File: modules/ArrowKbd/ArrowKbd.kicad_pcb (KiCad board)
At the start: 2 copper layers, 40.6 x 40.6 mm, 42 parts, among them J1 2, J10 11, J11 12, J12 13, J13 A0, J14 A1, J15 A2, J16 A3, J17 A4, J18 A5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

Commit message: ArrowKbd v2. Change pin assigning
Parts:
- moved JP1 20.2 mm to (120.7, 84.8), turned to 270 degrees
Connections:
- JP1 pad 1: Net-(J8-Pad1) -> Net-(J6-Pad1)
- JP1 pad 3: Net-(J7-Pad1) -> Net-(J3-Pad1)
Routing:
- net Net-(J6-Pad1): track 0.00 -> 20.9 mm
- net Net-(J3-Pad1): track 0.00 -> 20.4 mm
- net Net-(JP1-Pad2): track 55.9 -> 41.8 mm
- net Net-(J7-Pad1): track 3.59 -> 0.00 mm
- net Net-(J8-Pad1): track 2.54 -> 0.00 mm
- net Net-(D1-Pad2): track 37.9 -> 37.4 mm
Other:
- board text added: "hash"
- board text added: "v2"

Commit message: ArrowKbd. Add photomask in pdf.
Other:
- board text added: "c62680"
- board text removed: "hash"
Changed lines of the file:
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@@
     )
   )
-  (gr_text hash (at 117.475 89.2175) (layer F.Cu)
-    (effects (font (size 1.5 1.5) (thickness 0.3)))
+  (gr_text c62680 (at 118.11 89.2175) (layer F.Cu)
+    (effects (font (size 1 1) (thickness 0.2)))
   )
   (gr_text v2 (at 98.425 89.2175) (layer F.Cu)

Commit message: ArrowKbd. Update photomask in pdf.
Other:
- board text added: "747176"
- board text removed: "c62680"
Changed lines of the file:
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@@
     (visible_elements 7FFFFFFF)
     (pcbplotparams
-      (layerselection 0x010fc_ffffffff)
+      (layerselection 0x00000_fffffffe)
       (usegerberextensions false)
       (usegerberattributes false)
@@
       (hpglpenspeed 20)
       (hpglpendiameter 15.000000)
-      (psnegative false)
+      (psnegative true)
       (psa4output false)
       (plotreference true)
@@
       (padsonsilk false)
       (subtractmaskfromsilk false)
-      (outputformat 1)
+      (outputformat 4)
       (mirror false)
-      (drillshape 0)
+      (drillshape 1)
       (scaleselection 1)
-      (outputdirectory "arrowkbd/"))
+      (outputdirectory "pdf/"))
   )
   (net 0 "")
@@
     )
   )
-  (gr_text c62680 (at 118.11 89.2175) (layer F.Cu)
+  (gr_text 747176 (at 118.11 89.2175) (layer F.Cu)
     (effects (font (size 1 1) (thickness 0.2)))
   )

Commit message: ArrowKbd polishing
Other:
- board text added: "07.05.2020"
- board text added: "138553"
- board text removed: "04.03.2020"
- board text removed: "747176"
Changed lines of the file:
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@@
   )
   (setup
-    (last_trace_width 0.6)
+    (last_trace_width 0.25)
     (user_trace_width 0.4)
     (user_trace_width 0.5)
@@
     (mod_text_size 1 1)
     (mod_text_width 0.15)
-    (pad_size 1.524 1.524)
-    (pad_drill 0.762)
+    (pad_size 2 2)
+    (pad_drill 1)
     (pad_to_mask_clearance 0.051)
     (solder_mask_min_width 0.25)
@@
       (effects (font (size 1 1) (thickness 0.15)))
     )
-    (pad 1 thru_hole rect (at 0 0 270) (size 1.7 1.7) (drill 1) (layers *.Cu *.Mask)
+    (pad 1 thru_hole rect (at 0 0 270) (size 2 2) (drill 1) (layers *.Cu *.Mask)
       (net 6 "Net-(J6-Pad1)"))
-    (pad 2 thru_hole oval (at 0 2.54 270) (size 1.7 1.7) (drill 1) (layers *.Cu *.Mask)
+    (pad 2 thru_hole oval (at 0 2.54 270) (size 2 2) (drill 1) (layers *.Cu *.Mask)
       (net 29 "Net-(JP1-Pad2)"))
-    (pad 3 thru_hole oval (at 0 5.08 270) (size 1.7 1.7) (drill 1) (layers *.Cu *.Mask)
+    (pad 3 thru_hole oval (at 0 5.08 270) (size 2 2) (drill 1) (layers *.Cu *.Mask)
       (net 3 "Net-(J3-Pad1)"))
     (model ${KISYS3DMOD}/Connector_PinHeader_2.54mm.3dshapes/PinHeader_1x03_P2.54mm_Vertical.wrl
@@
     )
   )
-  (gr_text 747176 (at 118.11 89.2175) (layer F.Cu)
+  (gr_text 138553 (at 118.11 89.2175) (layer F.Cu)
     (effects (font (size 1 1) (thickness 0.2)))
   )
@@
   )
   (gr_poly (pts (xy 114.01 62.12) (xy 114.72 63.14) (xy 114.94 63.46) (xy 115.13 63.64) (xy 115.19 63.68) (xy 115.62 63.81) (xy 115.66 63.79) (xy 115.66 63.7) (xy 115.47 63.27) (xy 115.17 62.62) (xy 115.98 63.61) (xy 116.18 63.83) (xy 116.3 63.93) (xy 116.38 63.96) (xy 116.56 63.97) (xy 116.78 64.03) (xy 116.74 63.91) (xy 116.23 63.02) (xy 117 63.86) (xy 117.16 64.05) (xy 117.25 64.13) (xy 117.36 64.18) (xy 117.8 64.23) (xy 118.26 64.25) (xy 118.74 63.65) (xy 118.89 63.5) (xy 118.88 63.58) (xy 118.74 63.91) (xy 118.66 64.08) (xy 118.65 64.16) (xy 118.73 64.17) (xy 119.13 64.15) (xy 119.48 64.04) (xy 120.15 63.47) (xy 120.03 63.76) (xy 119.6 64.41) (xy 119.27 64.47) (xy 118.66 64.52) (xy 118.47 64.59) (xy 118.69 64.65) (xy 120.02 64.87) (xy 120.34 64.94) (xy 120.47 65.04) (xy 120.49 65.21) (xy 120.47 65.37) (xy 120.41 65.45) (xy 120.36 65.47) (xy 120.32 65.55) (xy 120.32 65.65) (xy 120.26 65.7) (xy 120.07 65.75) (xy 119.45 65.86) (xy 119.16 65.94) (xy 119.03 66.06) (xy 119 66.12) (xy 118.97 66.27) (xy 118.98 66.44) (xy 118.65 70.21) (xy 118.7 66.82) (xy 118.69 66.54) (xy 118.68 66.35) (xy 118.67 66.31) (xy 118.63 66.27) (xy 118.58 66.39) (xy 118.55 66.72) (xy 118.52 67.21) (xy 118.49 68.59) (xy 118.47 69.12) (xy 118.43 69.45) (xy 118.4 69.27) (xy 118.37 68.59) (xy 118.37 67.71) (xy 118.35 66.49) (xy 118.19 66.53) (xy 118.08 66.53) (xy 118.01 66.48) (xy 117.94 66.35) (xy 117.7 65.72) (xy 118.01 65.32) (xy 117.97 65.55) (xy 117.96 65.71) (xy 117.96 65.78) (xy 118.03 65.91) (xy 118.18 66.12) (xy 119.09 65.73) (xy 119.22 65.66) (xy 119.27 65.6) (xy 119.16 65.56) (xy 119.37 65.52) (xy 119.89 65.51) (xy 120.01 65.49) (xy 120.1 65.44) (xy 120.13 65.38) (xy 120.1 65.26) (xy 119.94 65.16) (xy 119.67 65.05) (xy 119.27 64.97) (xy 119.03 64.96) (xy 118.89 64.98) (xy 118.84 65.02) (xy 118.77 65.12) (xy 118.72 65.13) (xy 118.66 65.13) (xy 118.54 65.08) (xy 118.39 64.98) (xy 118.35 64.92) (xy 118.34 64.88) (xy 118.28 64.85) (xy 118.2 64.82) (xy 117.71 64.8) (xy 117.26 64.81) (xy 117.12 64.83) (xy 117 64.86) (xy 117.02 64.9) (xy 117.23 64.94) (xy 117.53 64.96) (xy 118.04 64.97) (xy 117.62 65.12) (xy 117.62 65.15) (xy 117.82 65.17) (xy 117.83 65.2) (xy 117.59 65.32) (xy 117.53 65.39) (xy 117.4 65.58) (xy 117.2 66.01) (xy 116.77 67.06) (xy 116.55 67.71) (xy 116.5 67.88) (xy 116.47 68.02) (xy 116.52 68.1) (xy 116.57 68.07) (xy 116.61 68) (xy 116.7 67.78) (xy 116.88 67.27) (xy 117.19 66.44) (xy 117.15 66.7) (xy 116.9 67.7) (xy 116.84 67.91) (xy 116.78 68.25) (xy 116.76 68.37) (xy 116.76 68.48) (xy 116.81 68.54) (xy 116.87 68.46) (xy 116.91 68.31) (xy 117.01 67.94) (xy 117.17 67.22) (xy 117.2 67.22) (xy 117.05 68.38) (xy 116.98 68.83) (xy 117.37 69.4) (xy 117.53 69.7) (xy 116.92 68.99) (xy 116.22 68.1) (xy 114.58 68.17) (xy 115.98 67.87) (xy 116.19 67.8) (xy 116.27 67.58) (xy 116.56 66.7) (xy 116.81 65.85) (xy 116.97 65.18) (xy 116.24 64.61) (xy 116.6 64.57) (xy 117.05 64.59) (xy 117.53 64.6) (xy 115.61 64.18) (xy 114.81 63.99) (xy 114.38 63.02)) (layer F.SilkS) (width 0.1))
-  (gr_text 04.03.2020 (at 103.1875 86.6775) (layer B.Cu)
-    (effects (font (size 1.5 1.5) (thickness 0.3)) (justify mirror))
+  (gr_text 07.05.2020 (at 100.6475 89.2175) (layer B.Cu)
+    (effects (font (size 1 1) (thickness 0.2)) (justify mirror))
   )
   (gr_text HardDuino (at 116.7 61) (layer F.SilkS)

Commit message: Fix 74LS139 pins
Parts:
- R1: moved to B.Cu
- moved R1 8.63 mm to (105.1, 75.2)
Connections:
- U1 pad 13: Net-(J11-Pad1) -> Net-(J12-Pad1)
- U1 pad 14: Net-(J12-Pad1) -> Net-(J11-Pad1)
- U1 pad 2: Net-(J12-Pad1) -> GND
- U1 pad 3: Net-(J11-Pad1) -> GND
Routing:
- net Net-(J12-Pad1): track 13.4 -> 59.2 mm, vias 0 -> 2
- net Net-(J16-Pad1): track 48.4 -> 67.9 mm
- net Net-(JP1-Pad2): track 41.8 -> 61.0 mm
- net Net-(D4-Pad2): track 27.6 -> 40.6 mm
- net Net-(D3-Pad2): track 36.9 -> 49.9 mm
- net Net-(D2-Pad2): track 18.1 -> 31.1 mm
- net Net-(J11-Pad1): track 14.6 -> 24.6 mm
- net VCC: track 47.4 -> 38.7 mm
- net Net-(D4-Pad1): track 13.6 -> 20.7 mm
- net Net-(D1-Pad2): track 37.4 -> 43.9 mm
- net Net-(D2-Pad1): track 15.6 -> 17.5 mm
- net Net-(D3-Pad1): track 15.1 -> 16.1 mm
- net GND: track 36.8 -> 37.7 mm, vias 2 -> 1
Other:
- board text added: "v2.1"
- board text removed: "v2"

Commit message: Fix hash, add gerber
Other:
- board text added: "07.11.2020"
- board text added: "cddc86"
- board text removed: "07.05.2020"
- board text removed: "138553"
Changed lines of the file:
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@@
   )
   (setup
-    (last_trace_width 0.6)
+    (last_trace_width 0.25)
     (user_trace_width 0.4)
     (user_trace_width 0.5)
@@
     (visible_elements 7FFFFFFF)
     (pcbplotparams
-      (layerselection 0x00000_fffffffe)
+      (layerselection 0x010f0_ffffffff)
       (usegerberextensions false)
       (usegerberattributes false)
@@
       (hpglpenspeed 20)
       (hpglpendiameter 15.000000)
-      (psnegative true)
+      (psnegative false)
       (psa4output false)
       (plotreference true)
@@
       (padsonsilk false)
       (subtractmaskfromsilk false)
-      (outputformat 4)
+      (outputformat 1)
       (mirror false)
-      (drillshape 1)
+      (drillshape 0)
       (scaleselection 1)
-      (outputdirectory "pdf/"))
+      (outputdirectory "gerber/"))
   )
   (net 0 "")
@@
       (effects (font (size 0.5 0.5) (thickness 0.08)) (justify mirror))
     )
-    (pad 1 smd roundrect (at -1.025 0 90) (size 1.15 1.4) (layers B.Cu B.Paste B.Mask) (roundrect_rratio 0.217391)
+    (pad 1 smd roundrect (at -1.025 0 90) (size 1.15 1.4) (layers B.Cu B.Paste B.Mask) (roundrect_rratio 0.2173904347826087)
       (net 19 VCC))
-    (pad 2 smd roundrect (at 1.025 0 90) (size 1.15 1.4) (layers B.Cu B.Paste B.Mask) (roundrect_rratio 0.217391)
+    (pad 2 smd roundrect (at 1.025 0 90) (size 1.15 1.4) (layers B.Cu B.Paste B.Mask) (roundrect_rratio 0.2173904347826087)
       (net 20 GND))
     (model ${KISYS3DMOD}/Capacitor_SMD.3dshapes/C_0805_2012Metric.wrl
@@
       (effects (font (size 0.5 0.5) (thickness 0.08)) (justify mirror))
     )
-    (pad 2 smd roundrect (at 1.025 0 270) (size 1.15 1.4) (layers B.Cu B.Paste B.Mask) (roundrect_rratio 0.217391)
+    (pad 2 smd roundrect (at 1.025 0 270) (size 1.15 1.4) (layers B.Cu B.Paste B.Mask) (roundrect_rratio 0.2173904347826087)
       (net 29 "Net-(JP1-Pad2)"))
-    (pad 1 smd roundrect (at -1.025 0 270) (size 1.15 1.4) (layers B.Cu B.Paste B.Mask) (roundrect_rratio 0.217391)
+    (pad 1 smd roundrect (at -1.025 0 270) (size 1.15 1.4) (layers B.Cu B.Paste B.Mask) (roundrect_rratio 0.2173904347826087)
       (net 19 VCC))
     (model ${KISYS3DMOD}/Resistor_SMD.3dshapes/R_0805_2012Metric.wrl
@@
       (effects (font (size 0.5 0.5) (thickness 0.08)))
     )
-    (pad 1 smd roundrect (at -1.025 0 180) (size 1.15 1.4) (layers F.Cu F.Paste F.Mask) (roundrect_rratio 0.217391)
+    (pad 1 smd roundrect (at -1.025 0 180) (size 1.15 1.4) (layers F.Cu F.Paste F.Mask) (roundrect_rratio 0.2173904347826087)
       (net 16 "Net-(J16-Pad1)"))
-    (pad 2 smd roundrect (at 1.025 0 180) (size 1.15 1.4) (layers F.Cu F.Paste F.Mask) (roundrect_rratio 0.217391)
+    (pad 2 smd roundrect (at 1.025 0 180) (size 1.15 1.4) (layers F.Cu F.Paste F.Mask) (roundrect_rratio 0.2173904347826087)
       (net 19 VCC))
     (model ${KISYS3DMOD}/Resistor_SMD.3dshapes/R_0805_2012Metric.wrl
@@
       (effects (font (size 0.5 0.5) (thickness 0.08)) (justify mirror))
     )
-    (pad 1 smd roundrect (at -1.025 0) (size 1.15 1.4) (layers B.Cu B.Paste B.Mask) (roundrect_rratio 0.217391)
+    (pad 1 smd roundrect (at -1.025 0) (size 1.15 1.4) (layers B.Cu B.Paste B.Mask) (roundrect_rratio 0.2173904347826087)
       (net 34 "Net-(R3-Pad1)"))
-    (pad 2 smd roundrect (at 1.025 0) (size 1.15 1.4) (layers B.Cu B.Paste B.Mask) (roundrect_rratio 0.217391)
+    (pad 2 smd roundrect (at 1.025 0) (size 1.15 1.4) (layers B.Cu B.Paste B.Mask) (roundrect_rratio 0.2173904347826087)
       (net 19 VCC))
     (model ${KISYS3DMOD}/Resistor_SMD.3dshapes/R_0805_2012Metric.wrl
@@
     )
   )
-  (gr_text 138553 (at 100.0125 86.995) (layer F.Cu)
+  (gr_text cddc86 (at 100.0125 86.995) (layer F.Cu)
     (effects (font (size 1 1) (thickness 0.2)))
   )
@@
   )
   (gr_poly (pts (xy 114.01 62.12) (xy 114.72 63.14) (xy 114.94 63.46) (xy 115.13 63.64) (xy 115.19 63.68) (xy 115.62 63.81) (xy 115.66 63.79) (xy 115.66 63.7) (xy 115.47 63.27) (xy 115.17 62.62) (xy 115.98 63.61) (xy 116.18 63.83) (xy 116.3 63.93) (xy 116.38 63.96) (xy 116.56 63.97) (xy 116.78 64.03) (xy 116.74 63.91) (xy 116.23 63.02) (xy 117 63.86) (xy 117.16 64.05) (xy 117.25 64.13) (xy 117.36 64.18) (xy 117.8 64.23) (xy 118.26 64.25) (xy 118.74 63.65) (xy 118.89 63.5) (xy 118.88 63.58) (xy 118.74 63.91) (xy 118.66 64.08) (xy 118.65 64.16) (xy 118.73 64.17) (xy 119.13 64.15) (xy 119.48 64.04) (xy 120.15 63.47) (xy 120.03 63.76) (xy 119.6 64.41) (xy 119.27 64.47) (xy 118.66 64.52) (xy 118.47 64.59) (xy 118.69 64.65) (xy 120.02 64.87) (xy 120.34 64.94) (xy 120.47 65.04) (xy 120.49 65.21) (xy 120.47 65.37) (xy 120.41 65.45) (xy 120.36 65.47) (xy 120.32 65.55) (xy 120.32 65.65) (xy 120.26 65.7) (xy 120.07 65.75) (xy 119.45 65.86) (xy 119.16 65.94) (xy 119.03 66.06) (xy 119 66.12) (xy 118.97 66.27) (xy 118.98 66.44) (xy 118.65 70.21) (xy 118.7 66.82) (xy 118.69 66.54) (xy 118.68 66.35) (xy 118.67 66.31) (xy 118.63 66.27) (xy 118.58 66.39) (xy 118.55 66.72) (xy 118.52 67.21) (xy 118.49 68.59) (xy 118.47 69.12) (xy 118.43 69.45) (xy 118.4 69.27) (xy 118.37 68.59) (xy 118.37 67.71) (xy 118.35 66.49) (xy 118.19 66.53) (xy 118.08 66.53) (xy 118.01 66.48) (xy 117.94 66.35) (xy 117.7 65.72) (xy 118.01 65.32) (xy 117.97 65.55) (xy 117.96 65.71) (xy 117.96 65.78) (xy 118.03 65.91) (xy 118.18 66.12) (xy 119.09 65.73) (xy 119.22 65.66) (xy 119.27 65.6) (xy 119.16 65.56) (xy 119.37 65.52) (xy 119.89 65.51) (xy 120.01 65.49) (xy 120.1 65.44) (xy 120.13 65.38) (xy 120.1 65.26) (xy 119.94 65.16) (xy 119.67 65.05) (xy 119.27 64.97) (xy 119.03 64.96) (xy 118.89 64.98) (xy 118.84 65.02) (xy 118.77 65.12) (xy 118.72 65.13) (xy 118.66 65.13) (xy 118.54 65.08) (xy 118.39 64.98) (xy 118.35 64.92) (xy 118.34 64.88) (xy 118.28 64.85) (xy 118.2 64.82) (xy 117.71 64.8) (xy 117.26 64.81) (xy 117.12 64.83) (xy 117 64.86) (xy 117.02 64.9) (xy 117.23 64.94) (xy 117.53 64.96) (xy 118.04 64.97) (xy 117.62 65.12) (xy 117.62 65.15) (xy 117.82 65.17) (xy 117.83 65.2) (xy 117.59 65.32) (xy 117.53 65.39) (xy 117.4 65.58) (xy 117.2 66.01) (xy 116.77 67.06) (xy 116.55 67.71) (xy 116.5 67.88) (xy 116.47 68.02) (xy 116.52 68.1) (xy 116.57 68.07) (xy 116.61 68) (xy 116.7 67.78) (xy 116.88 67.27) (xy 117.19 66.44) (xy 117.15 66.7) (xy 116.9 67.7) (xy 116.84 67.91) (xy 116.78 68.25) (xy 116.76 68.37) (xy 116.76 68.48) (xy 116.81 68.54) (xy 116.87 68.46) (xy 116.91 68.31) (xy 117.01 67.94) (xy 117.17 67.22) (xy 117.2 67.22) (xy 117.05 68.38) (xy 116.98 68.83) (xy 117.37 69.4) (xy 117.53 69.7) (xy 116.92 68.99) (xy 116.22 68.1) (xy 114.58 68.17) (xy 115.98 67.87) (xy 116.19 67.8) (xy 116.27 67.58) (xy 116.56 66.7) (xy 116.81 65.85) (xy 116.97 65.18) (xy 116.24 64.61) (xy 116.6 64.57) (xy 117.05 64.59) (xy 117.53 64.6) (xy 115.61 64.18) (xy 114.81 63.99) (xy 114.38 63.02)) (layer F.SilkS) (width 0.1))
-  (gr_text 07.05.2020 (at 100.33 89.2175) (layer B.Cu)
+  (gr_text 07.11.2020 (at 100.33 89.2175) (layer B.Cu)
     (effects (font (size 1 1) (thickness 0.2)) (justify mirror))
   )
@@
   (segment (start 90.17 83.185) (end 89.535 83.185) (width 0.3) (layer F.Cu) (net 0))
   (segment (start 89.535 83.185) (end 90.805 83.185) (width 0.3) (layer F.Cu) (net 0))
-  (via (at 109.5375 75.2475) (size 1.6) (drill 0.9) (layers F.Cu B.Cu) (net 12))
   (segment (start 121.92 86.995) (end 116.205 86.995) (width 0.6) (layer B.Cu) (net 3))
   (segment (start 123.825 77.47) (end 123.19 78.105) (width 0.6) (layer B.Cu) (net 3))
@@
   (segment (start 100.6475 67.6275) (end 100.33 67.31) (width 0.6) (layer B.Cu) (net 11))
   (segment (start 102.17 67.6275) (end 100.6475 67.6275) (width 0.6) (layer B.Cu) (net 11))
+  (via (at 109.5375 75.2475) (size 1.6) (drill 0.9) (layers F.Cu B.Cu) (net 12))
   (segment (start 94.16 64.77) (end 94.2975 64.9075) (width 0.6) (layer B.Cu) (net 12))
   (segment (start 92.71 64.77) (end 94.16 64.77) (width 0.6) (layer B.Cu) (net 12))

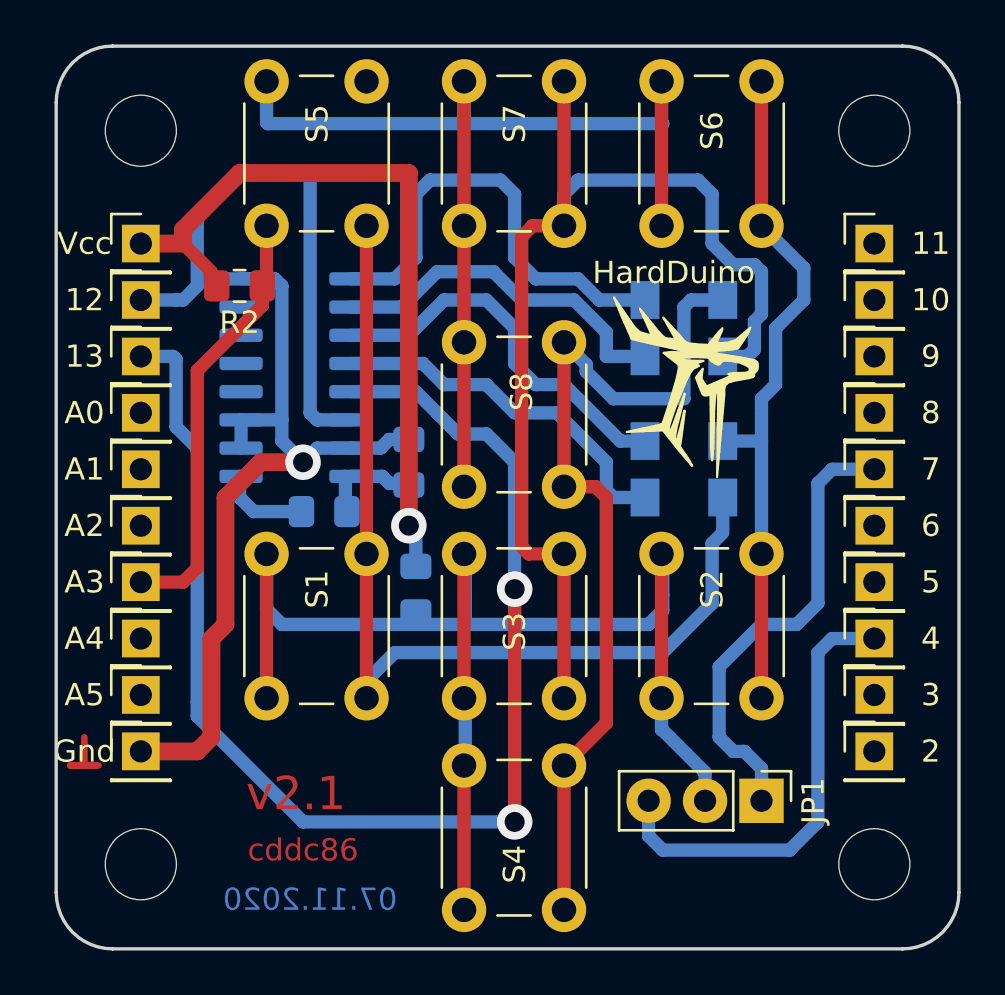
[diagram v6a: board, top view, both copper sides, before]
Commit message: 1x PCBs. Move holes to edges. Caution! This changes is uncompatible with previous versions...
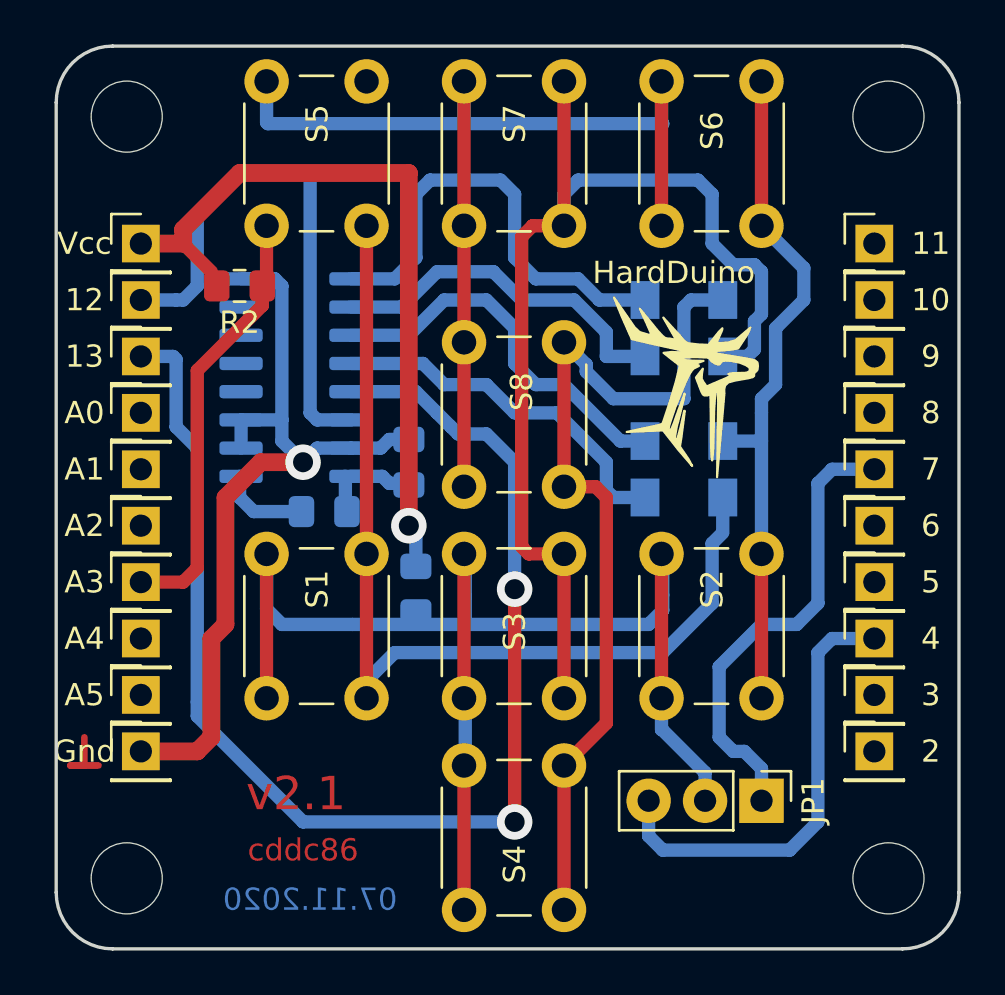
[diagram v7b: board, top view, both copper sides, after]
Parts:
- moved H2 0.90 mm to (92.1, 88.3)
- moved H4 0.90 mm to (126.4, 88.3)
- moved H1 0.90 mm to (92.1, 54.0)
- moved H3 0.90 mm to (126.4, 54.0)
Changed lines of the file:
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@@
   )
   (module MountingHole:MountingHole_3.2mm_M3 (layer F.Cu)
-    (at 92.71 54.61)
+    (at 92.0750 53.9750)
     (descr "Mounting Hole 3.2mm, no annular, M3")
     (tags "mounting hole 3.2mm no annular m3")
@@
   )
   (module MountingHole:MountingHole_3.2mm_M3 (layer F.Cu)
-    (at 92.71 87.63)
+    (at 92.0750 88.2650)
     (descr "Mounting Hole 3.2mm, no annular, M3")
     (tags "mounting hole 3.2mm no annular m3")
@@
   )
   (module MountingHole:MountingHole_3.2mm_M3 (layer F.Cu)
-    (at 125.73 54.61)
+    (at 126.3650 53.9750)
     (descr "Mounting Hole 3.2mm, no annular, M3")
     (tags "mounting hole 3.2mm no annular m3")
@@
   )
   (module MountingHole:MountingHole_3.2mm_M3 (layer F.Cu)
-    (at 125.73 87.63)
+    (at 126.3650 88.2650)
     (descr "Mounting Hole 3.2mm, no annular, M3")
     (tags "mounting hole 3.2mm no annular m3")

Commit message: Fix hash & version
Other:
- board text added: "21.02.2021"
- board text added: "b4d799"
- board text added: "v2.3"
- board text removed: "07.11.2020"
- board text removed: "cddc86"
- board text removed: "v2.1"
